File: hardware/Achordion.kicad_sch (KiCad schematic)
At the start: 55 parts, among them J1 Jack, J2 Jack, J3 Jack, J4 Jack, J5 Jack, J6 Jack, J7 Jack, J8 Power, SW1 Button, U1 Daisy_Patch_SM, U2 TL072

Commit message: Use a smaller capacitor footprint
Signed-off-by: Petr Horacek <petr@zlosynth.com>
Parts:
- C3, C4: footprint Capacitor_SMD:CP_Elec_6.3x5.8 -> Capacitor_SMD:CP_Elec_5x5.8
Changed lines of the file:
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@@
       (effects (font (size 1.27 1.27)) (justify left))
     )
-    (property "Footprint" "Capacitor_SMD:CP_Elec_6.3x5.8" (at 241.935 45.72 0)
+    (property "Footprint" "Capacitor_SMD:CP_Elec_5x5.8" (at 241.935 45.72 0)
       (effects (font (size 1.27 1.27)) hide)
     )
@@
       (effects (font (size 1.27 1.27)) (justify left))
     )
-    (property "Footprint" "Capacitor_SMD:CP_Elec_6.3x5.8" (at 241.935 38.1 0)
+    (property "Footprint" "Capacitor_SMD:CP_Elec_5x5.8" (at 241.935 38.1 0)
       (effects (font (size 1.27 1.27)) hide)
     )

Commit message: List more viable capacitors
Signed-off-by: Petr Horacek <petr@zlosynth.com>
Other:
- note added: "Low ESR caps 10u or 22u is fine"
- note removed: "Low ESR caps"
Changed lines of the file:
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@@
     (stroke (width 0) (type default))
   )
-  (text "Low ESR caps" (at 250.825 43.18 0)
+  (text "Low ESR caps\n10u or 22u is fine" (at 250.825 43.18 0)
     (effects (font (size 2.0066 2.0066)) (justify left bottom))
   )

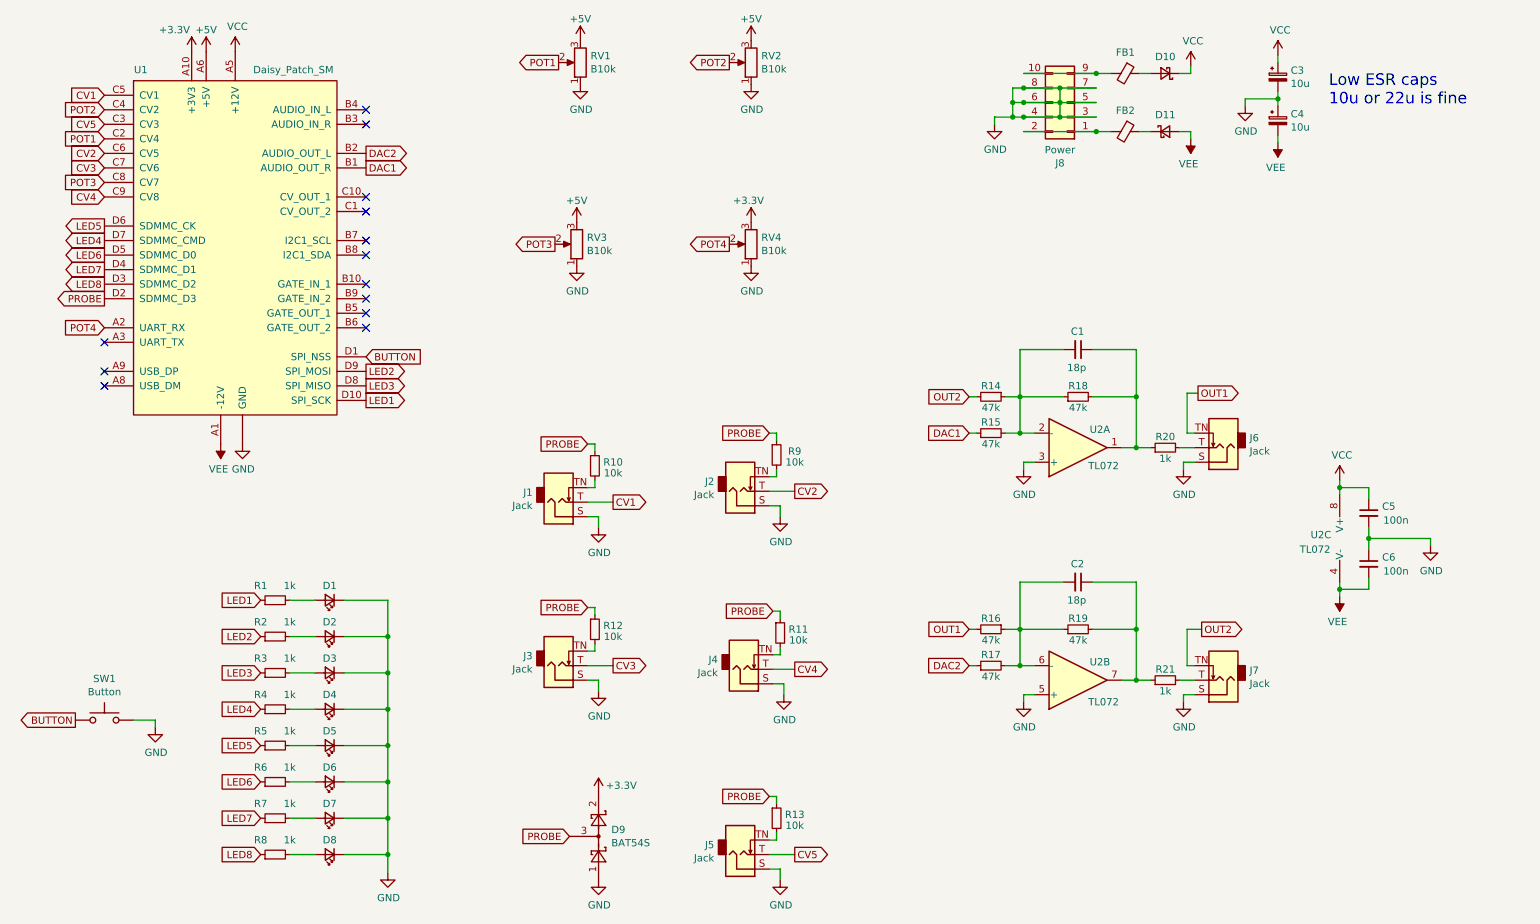
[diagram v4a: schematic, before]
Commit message: Use better footprints
This replaces the footprint of the power connector and the pots, making
them easier to solder in.

Signed-off-by: Petr Horacek <petr@zlosynth.com>
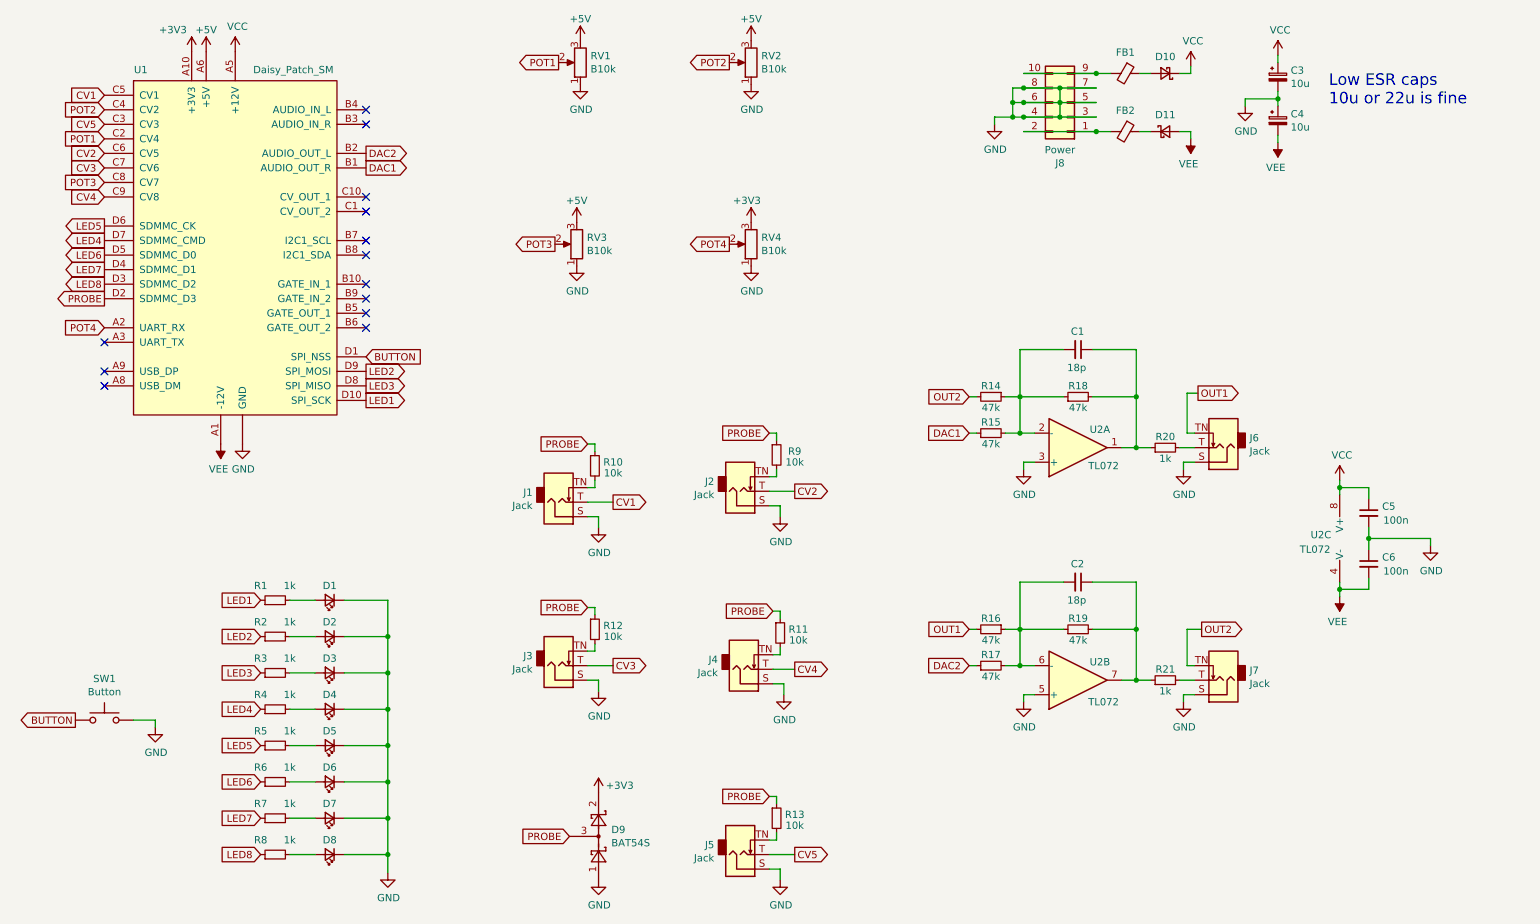
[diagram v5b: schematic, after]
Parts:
- FB1, FB2: footprint Inductor_SMD:L_0805_2012Metric_Pad1.15x1.40mm_HandSolder -> Inductor_SMD:L_0805_2012Metric_Pad1.05x1.20mm_HandSolder
- J8: footprint Connector_PinHeader_2.54mm:PinHeader_2x05_P2.54mm_Vertical -> BetterFootprints:Power_Connector_Connfly
- RV1, RV2, RV3, RV4: footprint Potentiometer_THT:Potentiometer_Alpha_RD901F-40-00D_Single_Vertical -> BetterFootprints:Potentiometer_Alpha
